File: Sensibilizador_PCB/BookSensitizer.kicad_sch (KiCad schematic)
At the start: 27 parts, among them U1 LM5104M, U2 LM5104M

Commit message: pequeño cambio
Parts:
- gave numbers to parts that had none: 1
- renumbered C3 to C4
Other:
- moved on the sheet: C3
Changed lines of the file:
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@@
   (junction (at 100.33 105.41) (diameter 0) (color 0 0 0 0)
   )
-  (junction (at 245.11 88.9) (diameter 0) (color 0 0 0 0)
-  )
   (junction (at 166.37 124.46) (diameter 0) (color 0 0 0 0)
   )
   (junction (at 44.45 88.9) (diameter 0) (color 0 0 0 0)
   )
-  (junction (at 245.11 124.46) (diameter 0) (color 0 0 0 0)
-  )
   (junction (at 200.66 96.52) (diameter 0) (color 0 0 0 0)
   )
@@
   (junction (at 97.79 96.52) (diameter 0) (color 0 0 0 0)
   )
+  (junction (at 247.65 124.46) (diameter 0) (color 0 0 0 0)
+  )
   (junction (at 100.33 88.9) (diameter 0) (color 0 0 0 0)
   )
+  (junction (at 247.65 88.9) (diameter 0) (color 0 0 0 0)
+  )
   (junction (at 194.31 124.46) (diameter 0) (color 0 0 0 0)
   )
@@
     (stroke (width 0) (type default) (color 0 0 0 0))
   )
+  (wire (pts (xy 247.65 88.9) (xy 257.81 88.9))
+    (stroke (width 0) (type default) (color 0 0 0 0))
+  )
   (wire (pts (xy 101.6 124.46) (xy 129.54 124.46))
     (stroke (width 0) (type default) (color 0 0 0 0))
@@
     (stroke (width 0) (type default) (color 0 0 0 0))
   )
-  (wire (pts (xy 245.11 107.95) (xy 245.11 124.46))
+  (wire (pts (xy 247.65 107.95) (xy 247.65 124.46))
     (stroke (width 0) (type default) (color 0 0 0 0))
   )
@@
     (stroke (width 0) (type default) (color 0 0 0 0))
   )
-  (wire (pts (xy 245.11 88.9) (xy 245.11 100.33))
+  (wire (pts (xy 247.65 88.9) (xy 247.65 100.33))
     (stroke (width 0) (type default) (color 0 0 0 0))
   )
@@
     (stroke (width 0) (type default) (color 0 0 0 0))
   )
-  (wire (pts (xy 245.11 88.9) (xy 257.81 88.9))
+  (wire (pts (xy 237.49 88.9) (xy 247.65 88.9))
     (stroke (width 0) (type default) (color 0 0 0 0))
   )
@@
     (stroke (width 0) (type default) (color 0 0 0 0))
   )
-  (wire (pts (xy 219.71 124.46) (xy 245.11 124.46))
+  (wire (pts (xy 219.71 124.46) (xy 247.65 124.46))
     (stroke (width 0) (type default) (color 0 0 0 0))
   )
@@
     (stroke (width 0) (type default) (color 0 0 0 0))
   )
+  (wire (pts (xy 237.49 96.52) (xy 240.03 96.52))
+    (stroke (width 0) (type default) (color 0 0 0 0))
+  )
   (wire (pts (xy 185.42 100.33) (xy 187.96 100.33))
     (stroke (width 0) (type default) (color 0 0 0 0))
   )
-  (wire (pts (xy 237.49 96.52) (xy 236.22 96.52))
-    (stroke (width 0) (type default) (color 0 0 0 0))
-  )
   (wire (pts (xy 119.38 82.55) (xy 119.38 88.9))
     (stroke (width 0) (type default) (color 0 0 0 0))
   )
-  (wire (pts (xy 237.49 88.9) (xy 245.11 88.9))
-    (stroke (width 0) (type default) (color 0 0 0 0))
-  )
   (wire (pts (xy 185.42 105.41) (xy 198.12 105.41))
     (stroke (width 0) (type default) (color 0 0 0 0))
   )
+  (wire (pts (xy 247.65 124.46) (xy 257.81 124.46))
+    (stroke (width 0) (type default) (color 0 0 0 0))
+  )
   (wire (pts (xy 180.34 88.9) (xy 176.53 88.9))
     (stroke (width 0) (type default) (color 0 0 0 0))
@@
   )
   (wire (pts (xy 118.11 82.55) (xy 119.38 82.55))
-    (stroke (width 0) (type default) (color 0 0 0 0))
-  )
-  (wire (pts (xy 245.11 124.46) (xy 257.81 124.46))
     (stroke (width 0) (type default) (color 0 0 0 0))
   )
@@
     (effects (font (size 1.27 1.27)) (justify left))
   )
-  (hierarchical_label "in_2" (shape input) (at 236.22 96.52 0)
+  (hierarchical_label "in_2" (shape input) (at 240.03 96.52 0)
     (effects (font (size 1.27 1.27)) (justify left))
   )
@@
   (symbol (lib_id "Device:C_Polarized") (at 257.81 104.14 0) (unit 1)
     (in_bom yes) (on_board yes)
-    (property "Reference" "C3" (id 0) (at 261.62 105.41 90)
+    (property "Reference" "C4" (id 0) (at 261.62 105.41 90)
       (effects (font (size 1.27 1.27)) (justify left))
     )
@@
     (pin "2")
   )
-  (symbol (lib_id "Device:C_Polarized") (at 245.11 104.14 0) (unit 1)
-    (in_bom yes) (on_board yes)
-    (property "Reference" "C?" (id 0) (at 251.46 105.41 90)
-      (effects (font (size 1.27 1.27)) (justify left))
-    )
-    (property "Value" "120nF 50V" (id 1) (at 248.92 109.22 90)
-      (effects (font (size 1.27 1.27)) (justify left))
-    )
-    (property "Footprint" "" (id 2) (at 246.0752 107.95 0)
-      (effects (font (size 1.27 1.27)) hide)
-    )
-    (property "Datasheet" "~" (id 3) (at 245.11 104.14 0)
+  (symbol (lib_id "Device:C_Polarized") (at 247.65 104.14 0) (unit 1)
+    (in_bom yes) (on_board yes)
+    (property "Reference" "C3" (id 0) (at 241.3 105.41 90)
+      (effects (font (size 1.27 1.27)) (justify left))
+    )
+    (property "Value" "120nF 50V" (id 1) (at 243.84 109.22 90)
+      (effects (font (size 1.27 1.27)) (justify left))
+    )
+    (property "Footprint" "" (id 2) (at 248.6152 107.95 0)
+      (effects (font (size 1.27 1.27)) hide)
+    )
+    (property "Datasheet" "~" (id 3) (at 247.65 104.14 0)
       (effects (font (size 1.27 1.27)) hide)
     )
@@
       (reference "C2") (unit 1) (value "120nF 50V") (footprint "")
     )
+    (path "/48faf4b4-702a-461e-beb4-48d0c1e72cc8"
+      (reference "C3") (unit 1) (value "120nF 50V") (footprint "")
+    )
     (path "/465bacb8-855b-413b-b25f-0e807e6db853"
-      (reference "C3") (unit 1) (value "2.7uF 50V") (footprint "")
-    )
-    (path "/48faf4b4-702a-461e-beb4-48d0c1e72cc8"
-      (reference "C?") (unit 1) (value "120nF 50V") (footprint "")
+      (reference "C4") (unit 1) (value "2.7uF 50V") (footprint "")
     )
     (path "/67aed173-e197-46ac-a867-f62a7f385d0c"

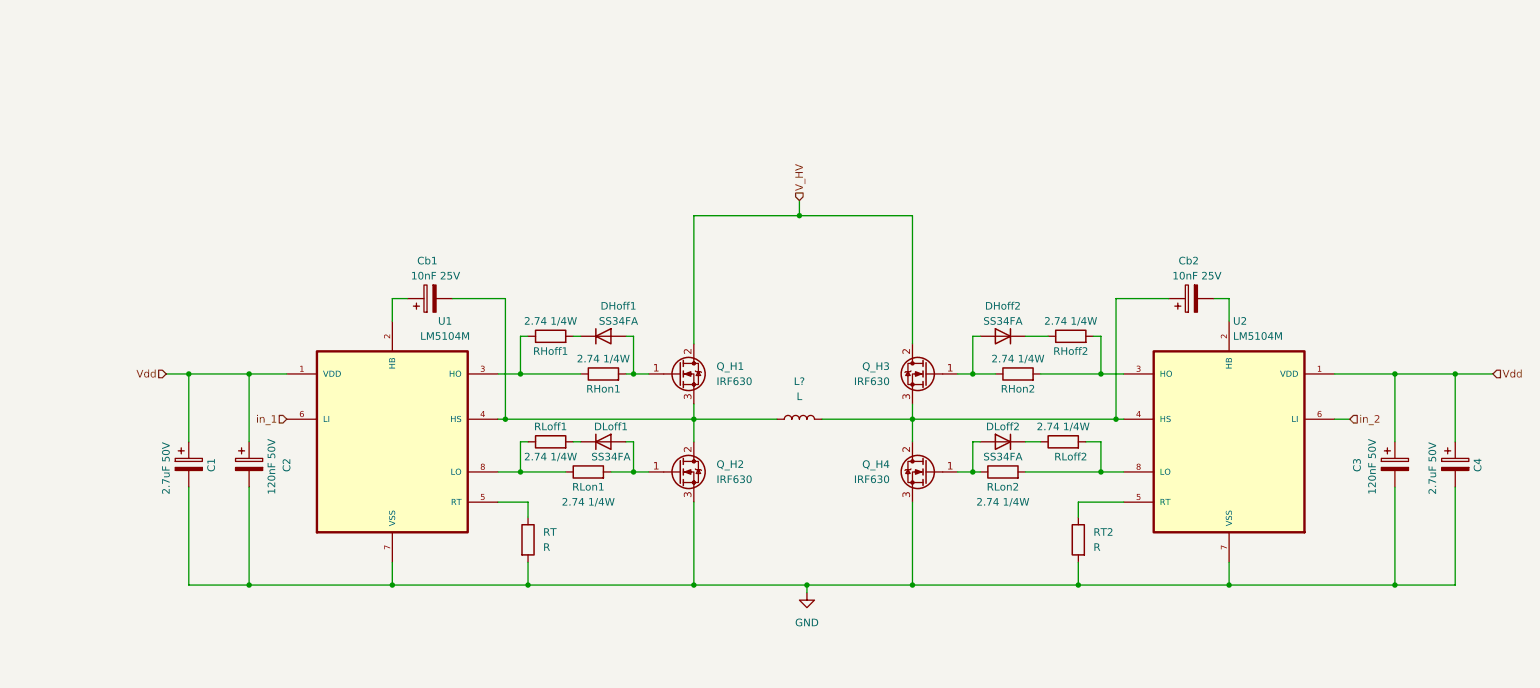
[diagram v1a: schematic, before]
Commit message: huellas agregadas
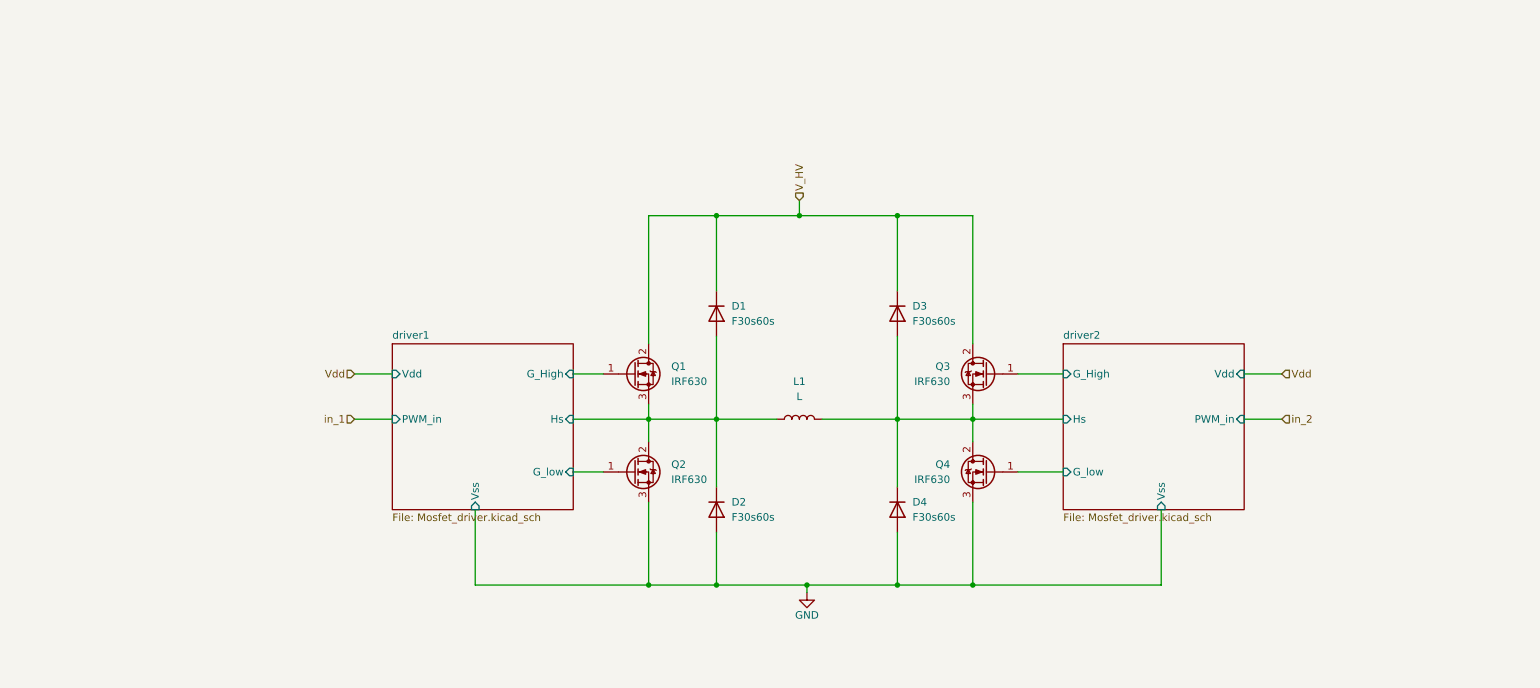
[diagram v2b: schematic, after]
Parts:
- removed C1, C4: 2.7uF 50V, symbol Device:C_Polarized
- removed C2, C3: 120nF 50V, symbol Device:C_Polarized
- removed Cb1, Cb2: 10nF 25V, symbol Device:C_Polarized
- removed DHoff1, DHoff2, DLoff1, DLoff2: SS34FA, symbol Device:D
- removed RHoff1, RHoff2, RHon1, RHon2, RLoff1, RLoff2, RLon1, RLon2: 2.74 1/4W, symbol Device:R
- removed RT, RT2: R, symbol Device:R
- removed U1, U2: LM5104M, SOIC127P599X175-8N, symbol LM5104M:LM5104M
- added D1, D2, D3, D4: F30s60s, Package_TO_SOT_THT:TO-220-2_Vertical, symbol Device:D
- L1: renamed from L?; footprint (none) -> Connector_Phoenix_MC_HighVoltage:PhoenixContact_MC_1,5_2-G-5.08_1x02_P5.08mm_Horizontal
- Q1: renamed from Q_H1; footprint (none) -> Package_TO_SOT_THT:TO-220-3_Vertical
- Q2: renamed from Q_H2; footprint (none) -> Package_TO_SOT_THT:TO-220-3_Vertical
- Q3: renamed from Q_H3; footprint (none) -> Package_TO_SOT_THT:TO-220-3_Vertical
- Q4: renamed from Q_H4; footprint (none) -> Package_TO_SOT_THT:TO-220-3_Vertical
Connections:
- net GND: now also D2.2 (A), D4.2 (A)
- net V_HV: now also D1.1 (K), D3.1 (K)
- net driver2/G_High: now reaches Q3.1 (G)
- net driver1/G_low: now reaches Q2.1 (G)
- net driver1/Hs: now reaches L1.1, Q1.3 (S), Q2.2 (D)
- net driver1/Hs: now also D1.2 (A), D2.1 (K)
- net driver2/Hs: now reaches L1.2, Q3.3 (S), Q4.2 (D)
- net driver2/Hs: now also D3.2 (A), D4.1 (K)
- net driver2/G_low: now reaches Q4.1 (G)
- net driver1/G_High: now reaches Q1.1 (G)
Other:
- added sheet driver1 (Mosfet_driver.kicad_sch)
- added sheet driver2 (Mosfet_driver.kicad_sch)
- moved on the sheet: Q1, Q2, Q3, Q4

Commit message: Rectificador primera versión
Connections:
- net V_HV renamed Rectificador/Vrect
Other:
- added sheet Rectificador (rectificador.kicad_sch)
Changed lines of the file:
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@@
     (stroke (width 0) (type default) (color 0 0 0 0))
   )
-  (wire (pts (xy 147.32 59.69) (xy 147.32 62.23))
+  (wire (pts (xy 147.32 50.8) (xy 147.32 62.23))
     (stroke (width 0) (type default) (color 0 0 0 0))
   )
@@
     (stroke (width 0) (type default) (color 0 0 0 0))
   )
+  (wire (pts (xy 78.74 50.8) (xy 147.32 50.8))
+    (stroke (width 0) (type default) (color 0 0 0 0))
+  )
   (wire (pts (xy 184.15 105.41) (xy 191.77 105.41))
     (stroke (width 0) (type default) (color 0 0 0 0))
@@
   )
   (wire (pts (xy 121.92 96.52) (xy 121.92 100.33))
+    (stroke (width 0) (type default) (color 0 0 0 0))
+  )
+  (wire (pts (xy 78.74 55.88) (xy 90.17 55.88))
     (stroke (width 0) (type default) (color 0 0 0 0))
   )
@@
     (effects (font (size 1.27 1.27)) (justify left))
   )
-  (hierarchical_label "V_HV" (shape input) (at 147.32 59.69 90)
-    (effects (font (size 1.27 1.27)) (justify left))
-  )
   (hierarchical_label "Vdd" (shape input) (at 72.39 88.9 180)
     (effects (font (size 1.27 1.27)) (justify right))
@@
     (pin "1")
     (pin "2")
+  )
+  (symbol (lib_id "power:GND") (at 90.17 55.88 0) (unit 1)
+    (in_bom yes) (on_board yes) (fields_autoplaced)
+    (property "Reference" "#PWR?" (id 0) (at 90.17 62.23 0)
+      (effects (font (size 1.27 1.27)) hide)
+    )
+    (property "Value" "GND" (id 1) (at 90.17 60.96 0))
+    (property "Footprint" "" (id 2) (at 90.17 55.88 0)
+      (effects (font (size 1.27 1.27)) hide)
+    )
+    (property "Datasheet" "" (id 3) (at 90.17 55.88 0)
+      (effects (font (size 1.27 1.27)) hide)
+    )
+    (pin "1")
   )
   (symbol (lib_id "Device:D") (at 163.83 111.76 270) (unit 1)
@@
     )
   )
+  (sheet (at 55.88 48.26) (size 22.86 10.16) (fields_autoplaced)
+    (stroke (width 0.1524) (type solid) (color 0 0 0 0))
+    (fill (color 0 0 0 0.0000))
+    (property "Sheet name" "Rectificador" (id 0) (at 55.88 47.5484 0)
+      (effects (font (size 1.27 1.27)) (justify left bottom))
+    )
+    (property "Sheet file" "rectificador.kicad_sch" (id 1) (at 55.88 59.0046 0)
+      (effects (font (size 1.27 1.27)) (justify left top))
+    )
+    (pin "Ref" input (at 78.74 55.88 0)
+      (effects (font (size 1.27 1.27)) (justify right))
+    )
+    (pin "Vrect" input (at 78.74 50.8 0)
+      (effects (font (size 1.27 1.27)) (justify right))
+    )
+  )
   (sheet (at 78.74 83.82) (size 30.48 27.94) (fields_autoplaced)
     (stroke (width 0.1524) (type solid) (color 0 0 0 0))
@@
     (path "/ac1f6bdf-cc2d-42eb-9880-0e22aa420d30" (page "2"))
     (path "/57202eac-790f-4d9e-a893-d48008c42ac0" (page "3"))
+    (path "/89b50e4b-0ad7-411a-9be3-4a266b580142" (page "4"))
   )
   (symbol_instances
+    (path "/4226d6b7-91fb-4f3c-8faf-45766a9fc25a"
+      (reference "#PWR?") (unit 1) (value "GND") (footprint "")
+    )
     (path "/947ef51d-b9f3-4316-a6d0-886a21eb9f2b"
       (reference "#PWR?") (unit 1) (value "GND") (footprint "")
@@
       (reference "C1") (unit 1) (value "1uF 50V") (footprint "Capacitor_SMD:C_Elec_4x5.4")
     )
+    (path "/89b50e4b-0ad7-411a-9be3-4a266b580142/ba697b81-73fc-47d2-81da-c085a6a00272"
+      (reference "C1") (unit 1) (value "C_Polarized") (footprint "")
+    )
     (path "/ac1f6bdf-cc2d-42eb-9880-0e22aa420d30/1d52d44f-853b-4d17-9aa5-e6400ac303d8"
       (reference "C2") (unit 1) (value "100nF 50V") (footprint "Capacitor_SMD:C_0603_1608Metric_Pad1.08x0.95mm_HandSolder")
@@
       (reference "D1") (unit 1) (value "F30s60s") (footprint "Package_TO_SOT_THT:TO-220-2_Vertical")
     )
+    (path "/89b50e4b-0ad7-411a-9be3-4a266b580142/2ed297ab-e72f-4059-9e52-401964eb63c0"
+      (reference "D1") (unit 1) (value "GBPC3506") (footprint "DIOB_GBPC3506")
+    )
     (path "/ac1f6bdf-cc2d-42eb-9880-0e22aa420d30/a9ae47de-03c4-4e71-a878-e0f67a7dba90"
       (reference "D1") (unit 1) (value "SS34FA") (footprint "Diode_SMD:D_SOD-123")
@@
       (reference "D?") (unit 1) (value "SS34FA") (footprint "Diode_SMD:D_SOD-123")
     )
+    (path "/89b50e4b-0ad7-411a-9be3-4a266b580142/0406db59-94a4-441e-b159-c1444bf42626"
+      (reference "J1") (unit 1) (value "Conn_01x02") (footprint "")
+    )
     (path "/d58551ab-7f8e-41c4-b486-4a9d9b32aa77"

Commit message: Listo pa tirar lineas
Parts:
- added F1: Fuse, Connector:porta_fusible, symbol Device:Fuse
- added J1: Jack_out, Connector_BarrelJack:BarrelJack_Horizontal, symbol Connector:Jack-DC
- added J2: Jack_in, Connector_BarrelJack:BarrelJack_Horizontal, symbol Connector:Jack-DC
- added J3: Conn_inputs, Connector_JST:JST_EH_S4B-EH_1x04_P2.50mm_Horizontal, symbol Connector:Conn_01x04_Male
- D1, D2, D3, D4: value F30s60s -> F10L60u
- L1: footprint Connector_Phoenix_MC_HighVoltage:PhoenixContact_MC_1,5_2-G-5.08_1x02_P5.08mm_Horizontal -> Connector:conector Faston
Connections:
- net GND: now also J1.2, J2.2, J3.4 (Pin_4)
- net in_1: now also J3.1 (Pin_1)
- net in_2: now also J3.2 (Pin_2)
- net Rectificador/Vrect renamed +12V
- net +12V: now also F1.2, J1.1
- new net: F1.1, J2.1
- new net in_3: J3.3 (Pin_3)
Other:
- removed sheet Rectificador
- added sheet ventilador (ventilador.kicad_sch)
- moved on the sheet: D1, L1, Q1, Q2, Q3, Q4

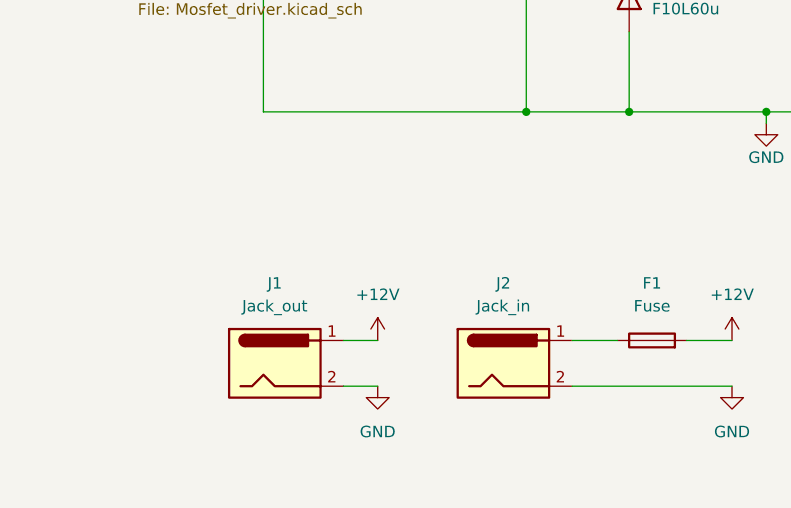
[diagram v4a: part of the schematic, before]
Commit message: mini cambio en label de RHon
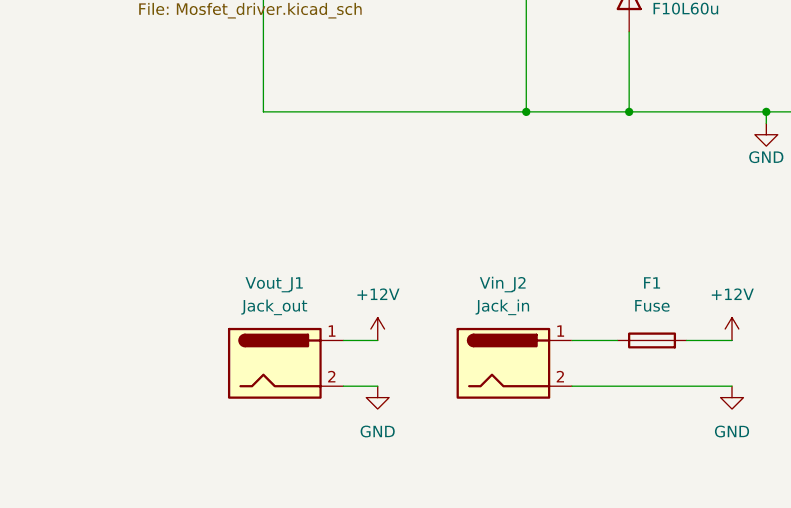
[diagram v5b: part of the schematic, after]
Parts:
- renumbered J2 to Vin_J2, J1 to Vout_J1
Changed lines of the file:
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@@
   (symbol (lib_id "Connector:Jack-DC") (at 43.18 125.73 0) (unit 1)
     (in_bom yes) (on_board yes) (fields_autoplaced)
-    (property "Reference" "J1" (id 0) (at 43.18 116.84 0))
+    (property "Reference" "Vout_J1" (id 0) (at 43.18 116.84 0))
     (property "Value" "Jack_out" (id 1) (at 43.18 119.38 0))
     (property "Footprint" "Connector_BarrelJack:BarrelJack_Horizontal" (id 2) (at 44.45 126.746 0)
@@
   (symbol (lib_id "Connector:Jack-DC") (at 68.58 125.73 0) (unit 1)
     (in_bom yes) (on_board yes) (fields_autoplaced)
-    (property "Reference" "J2" (id 0) (at 68.58 116.84 0))
+    (property "Reference" "Vin_J2" (id 0) (at 68.58 116.84 0))
     (property "Value" "Jack_in" (id 1) (at 68.58 119.38 0))
     (property "Footprint" "Connector_BarrelJack:BarrelJack_Horizontal" (id 2) (at 69.85 126.746 0)
@@
       (reference "F1") (unit 1) (value "Fuse") (footprint "Connector:porta_fusible")
     )
-    (path "/ad995c74-93e4-43e4-ae47-fc44625eb182"
-      (reference "J1") (unit 1) (value "Jack_out") (footprint "Connector_BarrelJack:BarrelJack_Horizontal")
-    )
-    (path "/f71f80e1-f664-4725-acdd-4c8e029873e4"
-      (reference "J2") (unit 1) (value "Jack_in") (footprint "Connector_BarrelJack:BarrelJack_Horizontal")
-    )
     (path "/2f75c6b7-af61-4db2-83bf-b2d5e7c5c4ff"
       (reference "J3") (unit 1) (value "Conn_inputs") (footprint "Connector_JST:JST_EH_S4B-EH_1x04_P2.50mm_Horizontal")
@@
     )
     (path "/ac1f6bdf-cc2d-42eb-9880-0e22aa420d30/e549455c-25cd-4632-8f00-16a0f558821b"
-      (reference "RHon1") (unit 1) (value " 2.74 1{slash}4W") (footprint "Resistor_SMD:R_1206_3216Metric_Pad1.30x1.75mm_HandSolder")
+      (reference "R9") (unit 1) (value " 2.74 1{slash}4W") (footprint "Resistor_SMD:R_1206_3216Metric_Pad1.30x1.75mm_HandSolder")
     )
     (path "/57202eac-790f-4d9e-a893-d48008c42ac0/e549455c-25cd-4632-8f00-16a0f558821b"
-      (reference "RHon2") (unit 1) (value " 2.74 1{slash}4W") (footprint "Resistor_SMD:R_1206_3216Metric_Pad1.30x1.75mm_HandSolder")
+      (reference "R10") (unit 1) (value " 2.74 1{slash}4W") (footprint "Resistor_SMD:R_1206_3216Metric_Pad1.30x1.75mm_HandSolder")
     )
     (path "/ac1f6bdf-cc2d-42eb-9880-0e22aa420d30/efbbbf4a-ba87-4fff-951e-42fd27464d32"
@@
       (reference "U2") (unit 1) (value "LM5104M") (footprint "Package_SO:SOIC-8_3.9x4.9mm_P1.27mm")
     )
-  )
+    (path "/f71f80e1-f664-4725-acdd-4c8e029873e4"
+      (reference "Vin_J2") (unit 1) (value "Jack_in") (footprint "Connector_BarrelJack:BarrelJack_Horizontal")
+    )
+    (path "/ad995c74-93e4-43e4-ae47-fc44625eb182"
+      (reference "Vout_J1") (unit 1) (value "Jack_out") (footprint "Connector_BarrelJack:BarrelJack_Horizontal")
+    )
+  )
